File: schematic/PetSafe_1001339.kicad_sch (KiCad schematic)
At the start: 150 parts, among them J1 ICSP, J3 PIR BOARD, J5 MOTOR, J6 DNP, Q1 FMOS3401A?, Q11 MMBTA55?, Q2 BC847B?, Q3 MMBTA55?, Q4 MMBTA55?, Q5 MMBTA55?, Q6 MMBTA55?, Q7 BC857C?, Q8 SIL3724A?, Q9 DNP, U1 S-1200B45?, U106 U6A / DNP, U2 SN74LVC2G14DBV?, U3 SGM8542XS, U4 PIC16F18855, U5 MX512H, U6 S-812C33AMC? / 3.3V, U7 DNP, Y1 20 MHz

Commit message: Reconstruct C6 in parallel with C5 from board photos
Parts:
- C5, C6: ConnectionEvidence (none) -> v0.9.18: C6 is reconstructed in parallel with C5 from the u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
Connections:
- net H_RF_VDD: now also C6.1
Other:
- note added: "C6 parallels C5 on H_RF_VDD/GND (photo-supported). Q8 F-P 10 ohm path still qualified."
- note added: "H07: C14R inverter candidate. C6 parallels C5 by photo; Q8 source rail still inferred."
- note added: "v0.9.18 | KiCad 10.0.5 | 2026-10-09"
- note removed: "C6: F-P 10 ohm, F-G 300 kohm suggests a supply-related node; exact path unresolved."
- note removed: "H07: C14R inverter candidate. Q8 source rail inferred; C6 destination unresolved."
- note removed: "v0.9.17 | KiCad 10.0.5 | 2026-10-09"

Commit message: Resolve receiver option wiring and measured D6 U6 connections
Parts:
- C42, R25, R47, R48: ConnectionEvidence (none) -> v0.9.19 user annotated local copper: R47 left -> U3.1/R27 r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
- D6: ConnectionEvidence (none) -> v0.9.20 B22-B27: upper photo contact V -> GND, lower W -> V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
- U6: ConnectionEvidence (none) -> v0.9.20: U6.5-U6.2 measured 1 ohm (B28). User annotation al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
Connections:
- net GND: now also C42.1, D6.2 (A); no longer R25.2
- net H_AUX_IN: now also U106.1 (Pin_1), U6.5 (NC)
- net MCLR_VPP: now also D6.1 (K)
- net VREF: no longer R48.2
- net at C22.1, R26.1, R27.2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: now also R47.1
- net RX_STAGE_LINK: now reaches R47.2
- net RX_STAGE_LINK: now also C42.2, R25.2, R48.2
- no-connect marks 0 -> 1
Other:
- note added: "D4/D5 ground returns photo-supported. D6: A=GND, K=VPP measured; breakdown unknown."
- note added: "U6: pin5 joins VIN (1 ohm); pin4 unused by user/photo. 3.3V is candidate rating."
- note added: "v0.9.20 | KiCad 10.0.5 | 2026-10-09"
- note removed: "D4/D5 opposite vias join rear GND copper. D6 type and routes remain uncertain."
- note removed: "U6: 3.3V is the candidate rating, not a voltage measurement. NC4/5 board ties unresolved."
- note removed: "v0.9.18 | KiCad 10.0.5 | 2026-10-09"
- moved on the sheet: C42, R47

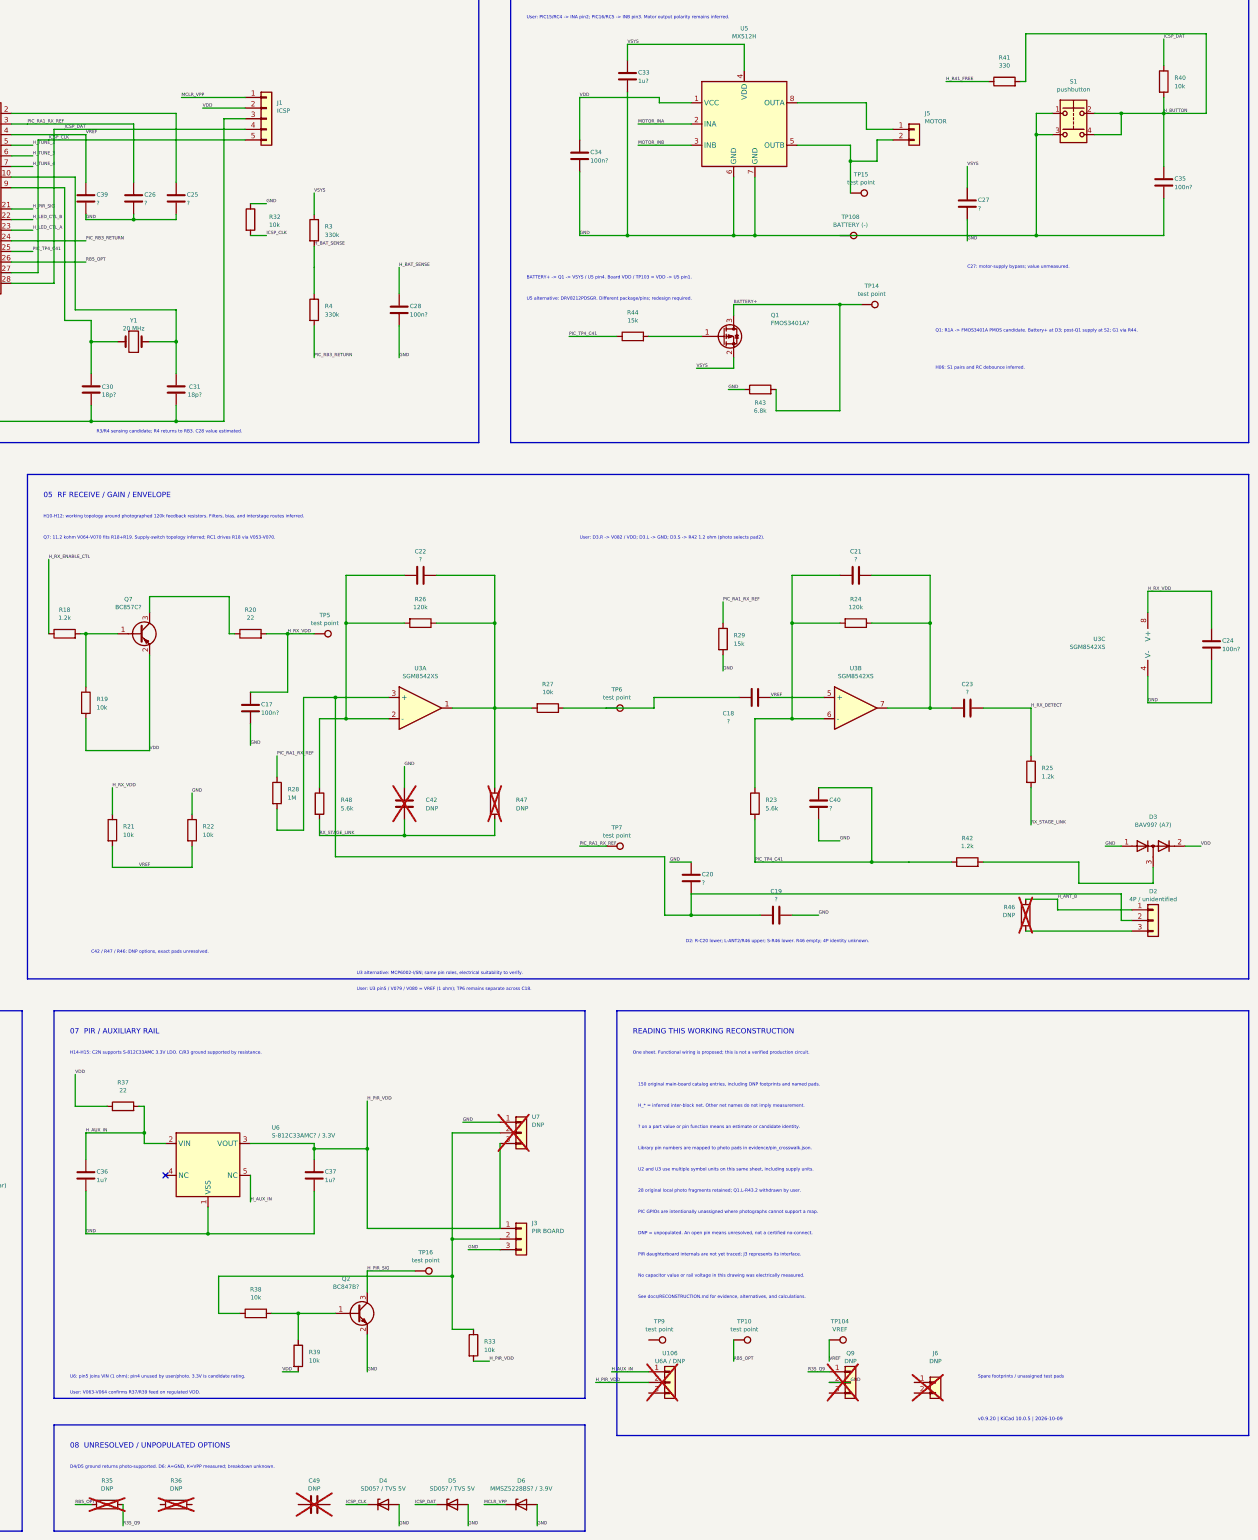
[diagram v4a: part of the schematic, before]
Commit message: Map J6 Q9 option and correct button routing to VPP
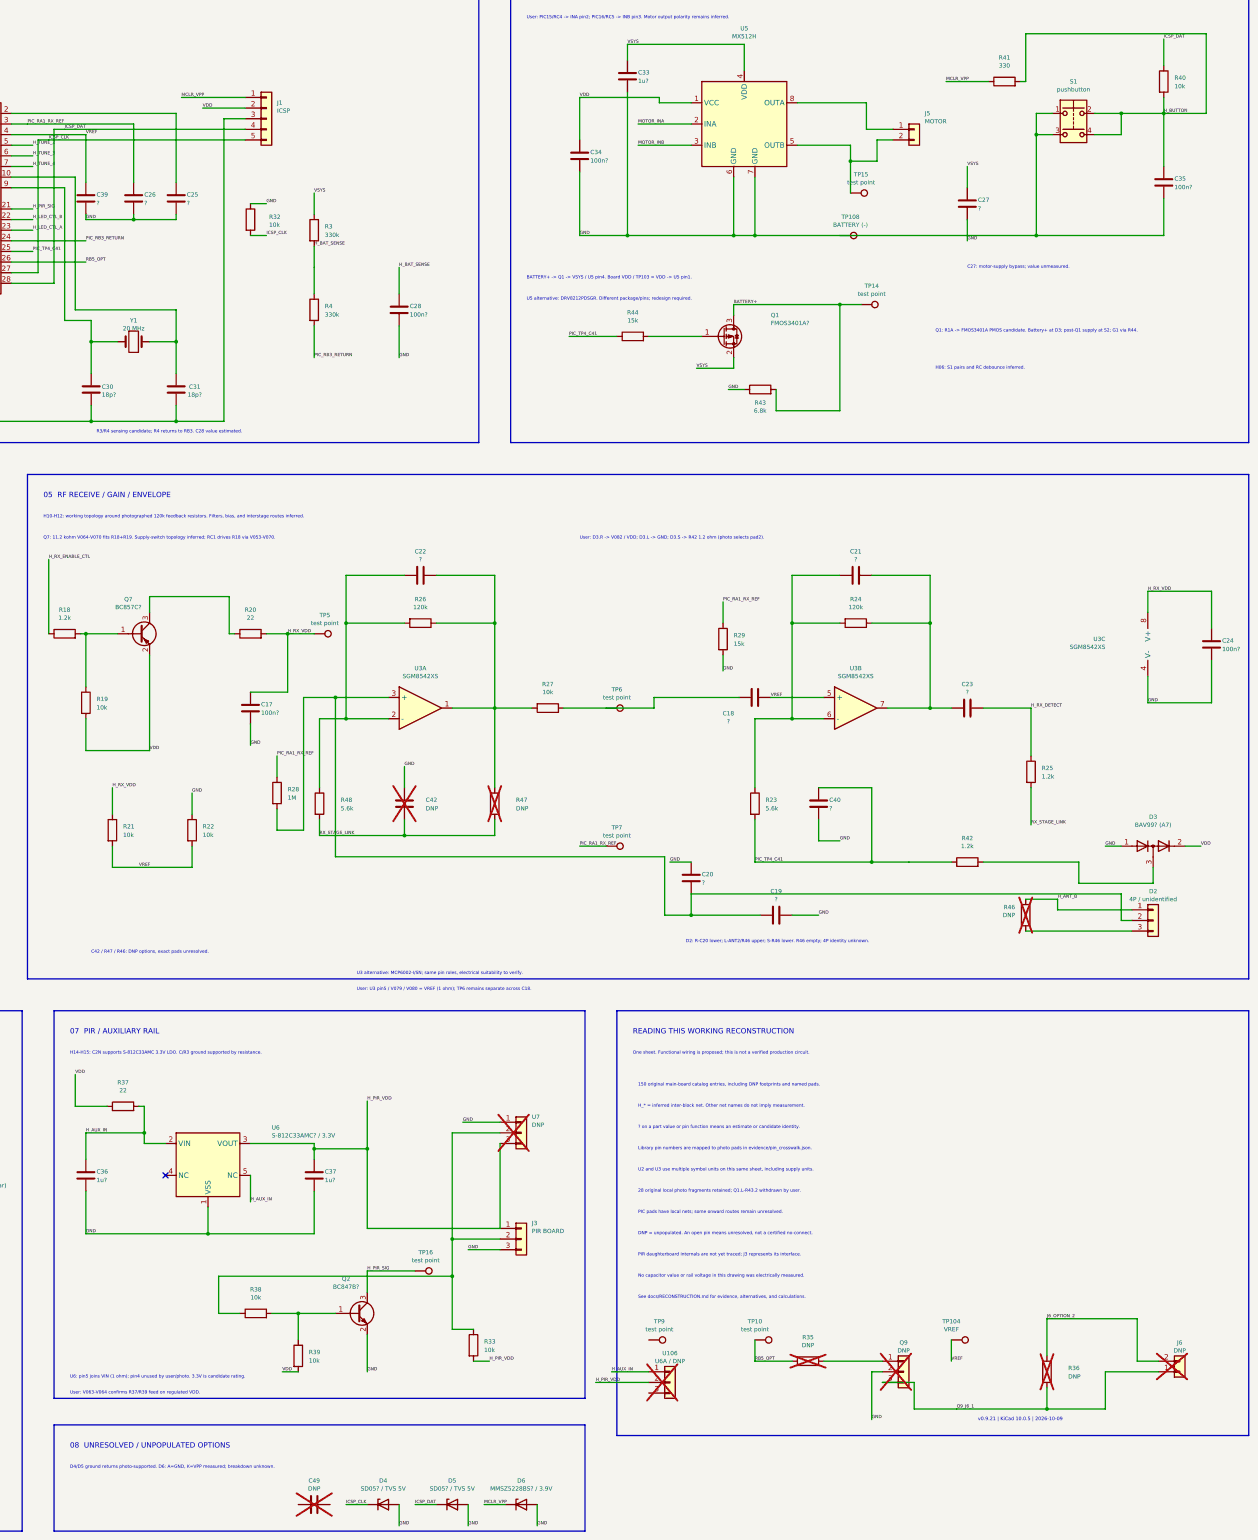
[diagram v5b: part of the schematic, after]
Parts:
- C35, R40, R41, S1: ConnectionEvidence (none) -> v0.9.21 user annotated S1 upper-right to C35 upper/model2 (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
- J6, Q9, R35, R36, TP10: ConnectionEvidence (none) -> v0.9.21 annotated photo: J6 left/model1 joins Q9 single/nat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
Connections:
- net H_R41_FREE is gone; now on net MCLR_VPP: R41.1
- net Q9_J6_1: now reaches Q9.3 (Pin_3)
- net Q9_J6_1: now also J6.1 (Pin_1), R36.2
- net J6_OPTION_2: now reaches R36.1
- net J6_OPTION_2: now also J6.2 (Pin_2)
- net R35_Q9: no longer names the net of Q9.1 (Pin_1), R35.2
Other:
- note added: "PIC pads have local nets; some onward routes remain unresolved."
- note added: "v0.9.21 | KiCad 10.0.5 | 2026-10-09"
- note removed: "PIC GPIOs are intentionally unassigned where photographs cannot support a map."
- note removed: "Spare footprints / unassigned test pads"
- note removed: "v0.9.20 | KiCad 10.0.5 | 2026-10-09"
- moved on the sheet: J6, Q9, R35, R36, TP10, TP104

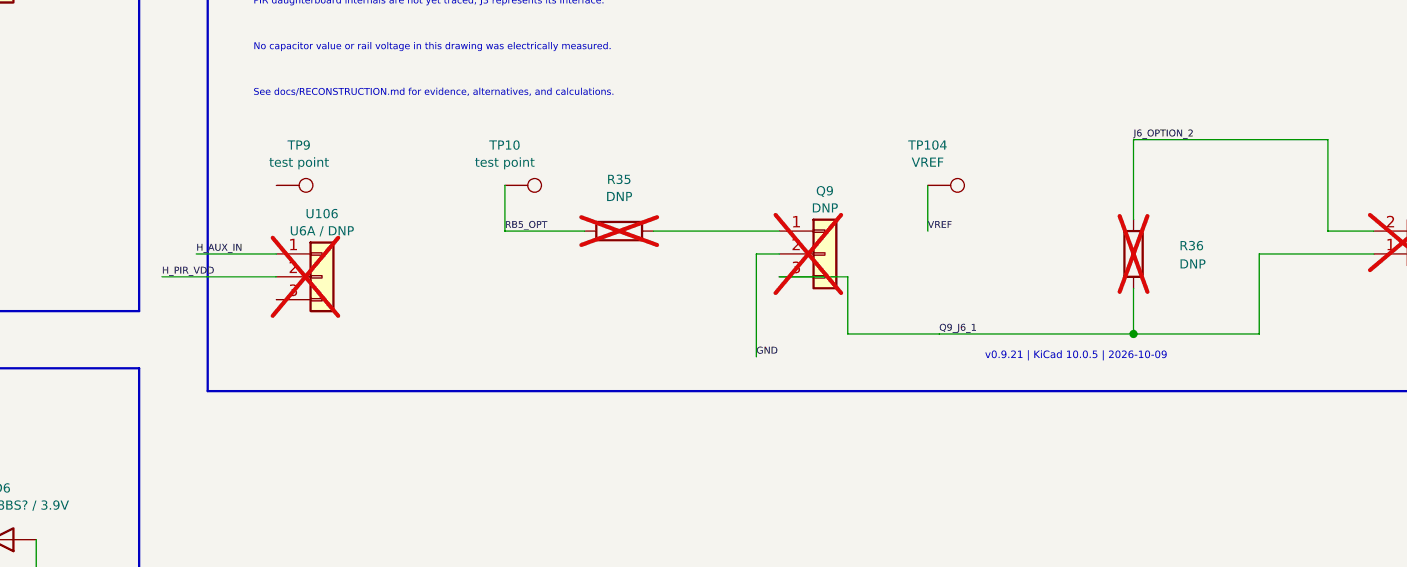
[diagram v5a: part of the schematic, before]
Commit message: Complete U6A option pad mapping with confirmed ground
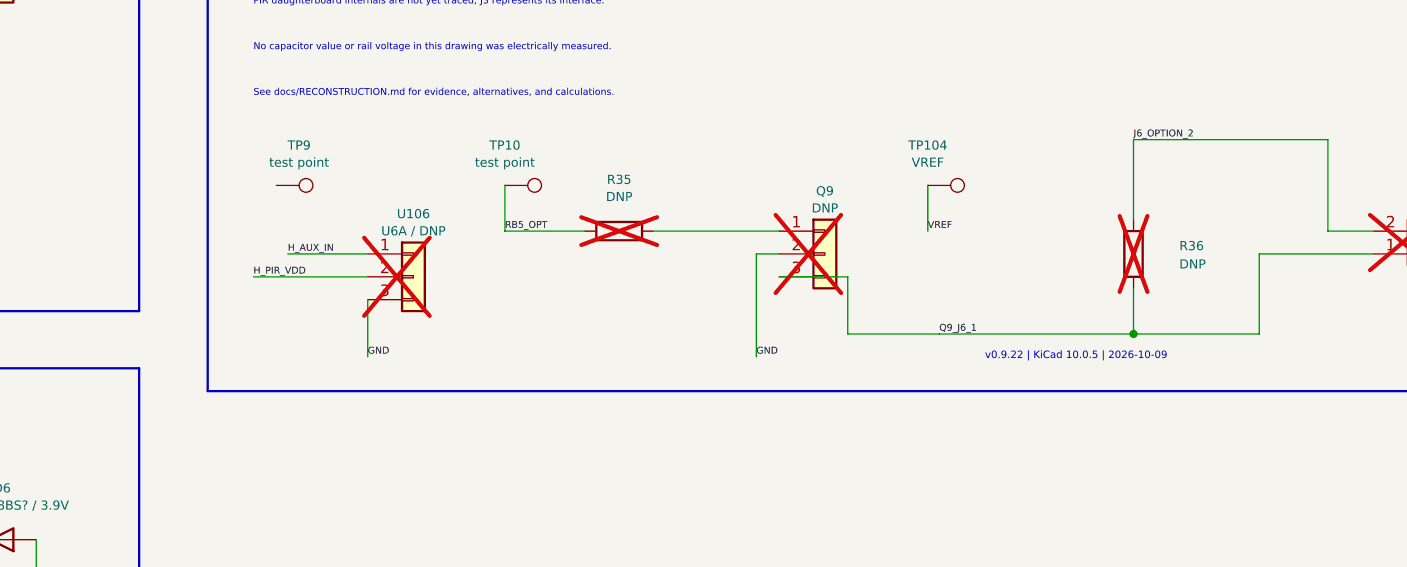
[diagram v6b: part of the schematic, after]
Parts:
- U106: ConnectionEvidence (none) -> v0.9.22 user annotated U6A option: single left pad/model L/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
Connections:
- net GND: now also U106.3 (Pin_3)
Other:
- note added: "v0.9.22 | KiCad 10.0.5 | 2026-10-09"
- note removed: "v0.9.21 | KiCad 10.0.5 | 2026-10-09"
- moved on the sheet: U106

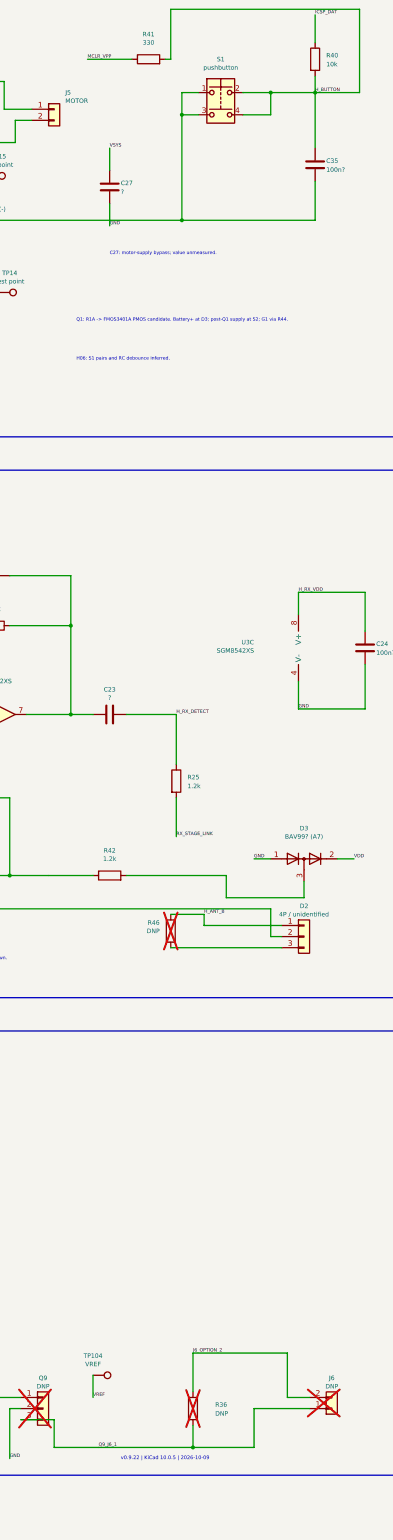
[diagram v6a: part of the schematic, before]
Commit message: Assign stock S1 tactile footprint from measured body dimensions
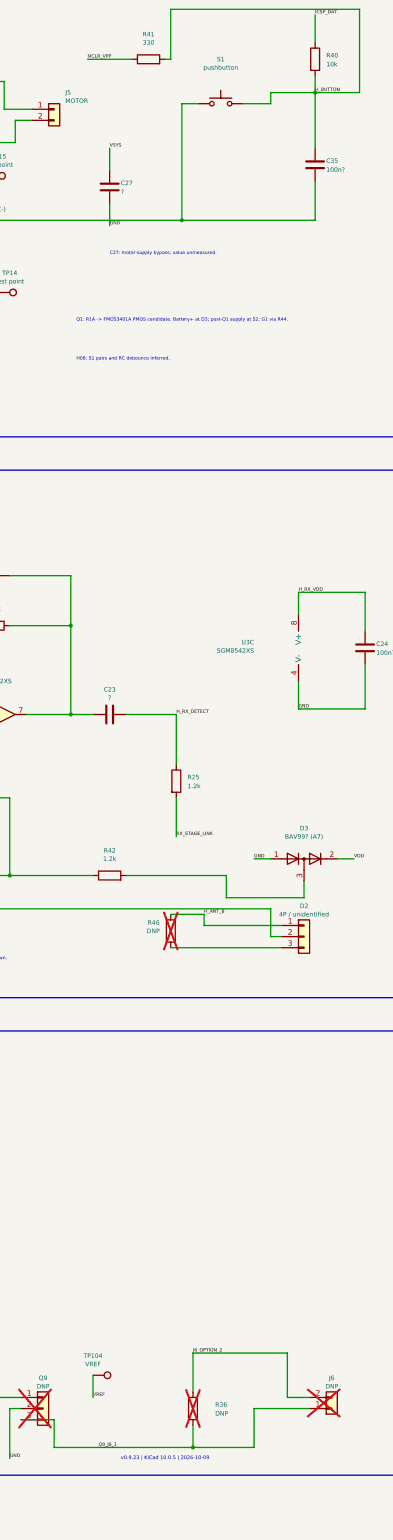
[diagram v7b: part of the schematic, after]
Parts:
- removed S1: pushbutton, symbol Switch:SW_Push_Dual
- added S1: pushbutton, Button_Switch_SMD:SW_SPST_PTS645Sx43SMTR92, symbol Switch:SW_Push
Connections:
- net GND: now also S1.1
- net H_BUTTON: now also S1.2
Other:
- note added: "v0.9.23 | KiCad 10.0.5 | 2026-10-09"
- note removed: "v0.9.22 | KiCad 10.0.5 | 2026-10-09"

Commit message: Group optional circuits by function and replace device placeholders
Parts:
- removed Q9: DNP, Package_TO_SOT_SMD:SOT-23, symbol Connector_Generic:Conn_01x03
- removed TP9: test point, TestPoint:TestPoint_THTPad_D2.0mm_Drill1.0mm, symbol Connector:TestPoint
- removed U106: U6A / DNP, Package_TO_SOT_SMD:SOT-23, symbol Connector_Generic:Conn_01x03
- added Q9: NPN option / DNP, Package_TO_SOT_SMD:SOT-23, symbol Transistor_BJT:Q_NPN_BEC
- added U106: U6A / LDO option, Package_TO_SOT_SMD:SOT-23, symbol Regulator_Linear:MCP1700x-330xxTT
- C49: LocationEvidence (none) -> Clearly visible empty C49 on rear IMG_2442.jpg beside anten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
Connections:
- net GND: now also Q9.2 (E), U106.1 (GND)
- net H_AUX_IN: now also U106.3 (VI)
- net H_PIR_VDD: now also U106.2 (VO)
- net Q9_J6_1: now also Q9.3 (C)
- net at R35.2: now also Q9.1 (B)
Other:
- note added: "149 retained catalog entries; unsupported TP9 entry removed after photo audit."
- note added: "U6A: DNP alternative regulator; stock symbol does not identify the original part."
- note added: "v0.9.24 | KiCad 10.0.5 | 2026-10-09"
- note removed: "08 UNRESOLVED / UNPOPULATED OPTIONS"
- note removed: "150 original main-board catalog entries, including DNP footprints and named pads."
- note removed: "D4/D5 ground returns photo-supported. D6: A=GND, K=VPP measured; breakdown unknown."
- note removed: "User: V063-V064 confirms R37/R39 feed on regulated VDD."
- note removed: "v0.9.23 | KiCad 10.0.5 | 2026-10-09"
- moved on the sheet: C49, D4, D5, D6, J6, R35, R36, TP10, TP104
